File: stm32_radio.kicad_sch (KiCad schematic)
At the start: 3 parts, among them J1 Conn_01x03_Pin, J2 Conn_Coaxial_Small

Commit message: Almost ready for production
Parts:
- J1: LCSC (none) -> C49257
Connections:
- no-connect marks 25 -> 23
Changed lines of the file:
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@@
 	)
 	(junction
-		(at 38.1 143.51)
+		(at 66.04 110.49)
 		(diameter 0)
 		(color 0 0 0 0)
@@
 	)
 	(no_connect
-		(at 60.96 62.23)
-	)
-	(no_connect
 		(at 60.96 73.66)
 	)
@@
 	)
 	(no_connect
-		(at 60.96 59.69)
-	)
-	(no_connect
 		(at 60.96 76.2)
 	)
@@
 	(wire
 		(pts
-			(xy 38.1 143.51) (xy 38.1 144.78)
+			(xy 38.1 139.7) (xy 38.1 144.78)
 		)
 		(stroke
@@
 		(pts
 			(xy 60.96 119.38) (xy 71.12 119.38)
-		)
-		(stroke
-			(width 0)
-			(type default)
-		)
-	)
-	(wire
-		(pts
-			(xy 38.1 139.7) (xy 38.1 143.51)
 		)
 		(stroke
@@
 	)
 	(symbol
-		(lib_id "Connector:Conn_01x03_Pin")
-		(at 71.12 105.41 270)
+		(lib_id "power:PWR_FLAG")
+		(at 66.04 110.49 0)
 		(unit 1)
 		(exclude_from_sim no)
@@
 		(dnp no)
 		(fields_autoplaced yes)
-		(property "Reference" "J1"
-			(at 71.12 100.33 90)
-			(effects
-				(font
-					(size 1.27 1.27)
-				)
-			)
-		)
-		(property "Value" "Conn_01x03_Pin"
-			(at 71.12 102.87 90)
-			(effects
-				(font
-					(size 1.27 1.27)
-				)
-			)
-		)
-		(property "Footprint" "Connector_PinHeader_2.54mm:PinHeader_1x03_P2.54mm_Vertical"
-			(at 71.12 105.41 0)
+		(property "Reference" "#FLG05"
+			(at 66.04 108.585 0)
+			(effects
+				(font
+					(size 1.27 1.27)
+				)
+				(hide yes)
+			)
+		)
+		(property "Value" "PWR_FLAG"
+			(at 66.04 105.41 0)
+			(effects
+				(font
+					(size 1.27 1.27)
+				)
+			)
+		)
+		(property "Footprint" ""
+			(at 66.04 110.49 0)
 			(effects
 				(font
@@
 		)
 		(property "Datasheet" "~"
-			(at 71.12 105.41 0)
-			(effects
-				(font
-					(size 1.27 1.27)
-				)
-				(hide yes)
-			)
-		)
-		(property "Description" "Generic connector, single row, 01x03, script generated"
-			(at 71.12 105.41 0)
+			(at 66.04 110.49 0)
+			(effects
+				(font
+					(size 1.27 1.27)
+				)
+				(hide yes)
+			)
+		)
+		(property "Description" "Special symbol for telling ERC where power comes from"
+			(at 66.04 110.49 0)
 			(effects
 				(font
@@
 		(pin "1"
 		)
-		(pin "3"
-		)
-		(pin "2"
-		)
 		(instances
-			(project ""
+			(project "stm32_radio"
 				(path "/432d5beb-0309-422b-bb62-0445459d5147"
-					(reference "J1")
+					(reference "#FLG05")
 					(unit 1)
 				)
@@
 	)
 	(symbol
-		(lib_id "power:PWR_FLAG")
-		(at 38.1 143.51 90)
+		(lib_id "Connector:Conn_01x03_Pin")
+		(at 71.12 105.41 270)
 		(unit 1)
 		(exclude_from_sim no)
@@
 		(dnp no)
 		(fields_autoplaced yes)
-		(property "Reference" "#FLG01"
-			(at 36.195 143.51 0)
-			(effects
-				(font
-					(size 1.27 1.27)
-				)
-				(hide yes)
-			)
-		)
-		(property "Value" "PWR_FLAG"
-			(at 34.29 143.5099 90)
-			(effects
-				(font
-					(size 1.27 1.27)
-				)
-				(justify left)
-			)
-		)
-		(property "Footprint" ""
-			(at 38.1 143.51 0)
+		(property "Reference" "J1"
+			(at 71.12 100.33 90)
+			(effects
+				(font
+					(size 1.27 1.27)
+				)
+			)
+		)
+		(property "Value" "Conn_01x03_Pin"
+			(at 71.12 102.87 90)
+			(effects
+				(font
+					(size 1.27 1.27)
+				)
+			)
+		)
+		(property "Footprint" "Connector_PinHeader_2.54mm:PinHeader_1x03_P2.54mm_Vertical"
+			(at 71.12 105.41 0)
 			(effects
 				(font
@@
 		)
 		(property "Datasheet" "~"
-			(at 38.1 143.51 0)
-			(effects
-				(font
-					(size 1.27 1.27)
-				)
-				(hide yes)
-			)
-		)
-		(property "Description" "Special symbol for telling ERC where power comes from"
-			(at 38.1 143.51 0)
-			(effects
-				(font
-					(size 1.27 1.27)
-				)
-				(hide yes)
+			(at 71.12 105.41 0)
+			(effects
+				(font
+					(size 1.27 1.27)
+				)
+				(hide yes)
+			)
+		)
+		(property "Description" "Generic connector, single row, 01x03, script generated"
+			(at 71.12 105.41 0)
+			(effects
+				(font
+					(size 1.27 1.27)
+				)
+				(hide yes)
+			)
+		)
+		(property "LCSC" "C49257"
+			(at 71.12 105.41 0)
+			(effects
+				(font
+					(size 1.27 1.27)
+				)
 			)
 		)
 		(pin "1"
+		)
+		(pin "3"
+		)
+		(pin "2"
 		)
 		(instances
 			(project ""
 				(path "/432d5beb-0309-422b-bb62-0445459d5147"
-					(reference "#FLG01")
+					(reference "J1")
 					(unit 1)
 				)

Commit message: Finalize design
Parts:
- removed J1: Conn_01x03_Pin, Connector_PinHeader_2.54mm:PinHeader_1x03_P2.54mm_Vertical, symbol Connector:Conn_01x03_Pin

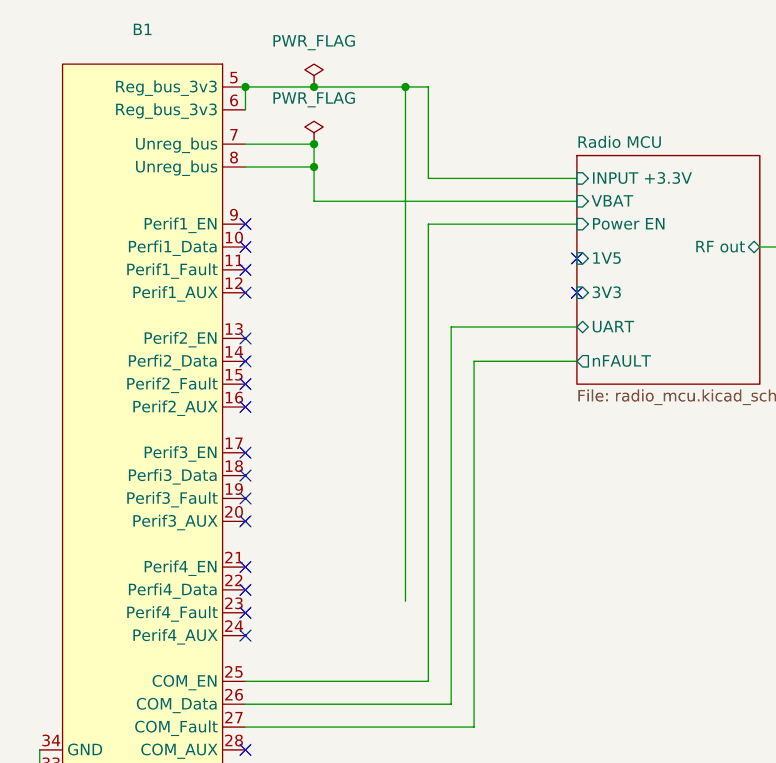
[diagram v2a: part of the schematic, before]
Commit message: Altered LCSC part numbers according to current stock
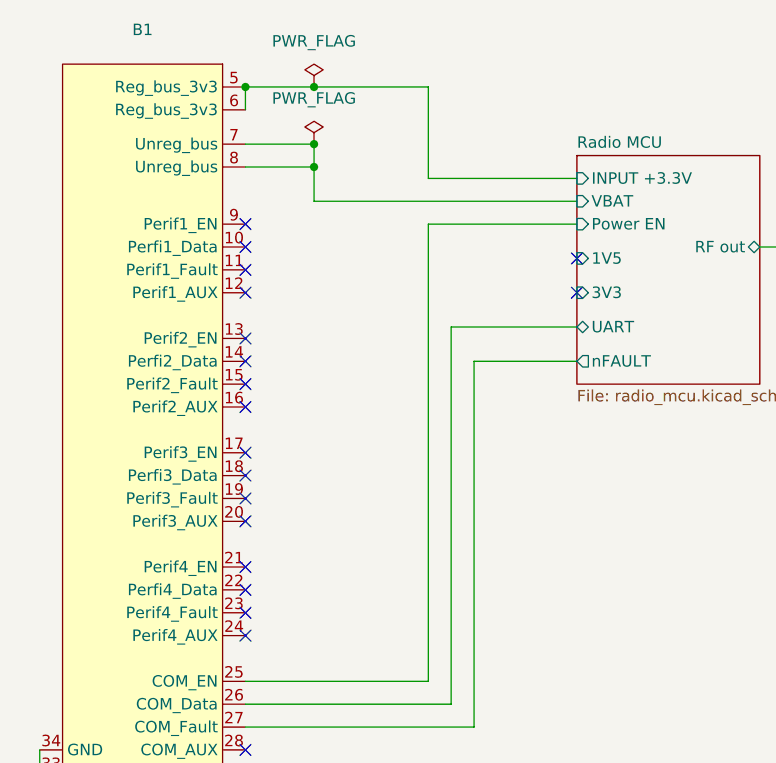
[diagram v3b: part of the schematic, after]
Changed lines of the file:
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@@
-	)
-	(junction
-		(at 78.74 53.34)
-		(diameter 0)
-		(color 0 0 0 0)
 	)
 	(junction
@@
 	(wire
 		(pts
-			(xy 68.58 53.34) (xy 78.74 53.34)
-		)
-		(stroke
-			(width 0)
-			(type default)
-		)
-	)
-	(wire
-		(pts
 			(xy 138.43 71.12) (xy 138.43 72.39)
 		)
@@
 	(wire
 		(pts
-			(xy 78.74 53.34) (xy 78.74 110.49)
-		)
-		(stroke
-			(width 0)
-			(type default)
-		)
-	)
-	(wire
-		(pts
 			(xy 83.82 80.01) (xy 97.79 80.01)
 		)
@@
 	(wire
 		(pts
-			(xy 81.28 53.34) (xy 78.74 53.34)
+			(xy 68.58 53.34) (xy 81.28 53.34)
 		)
 		(stroke

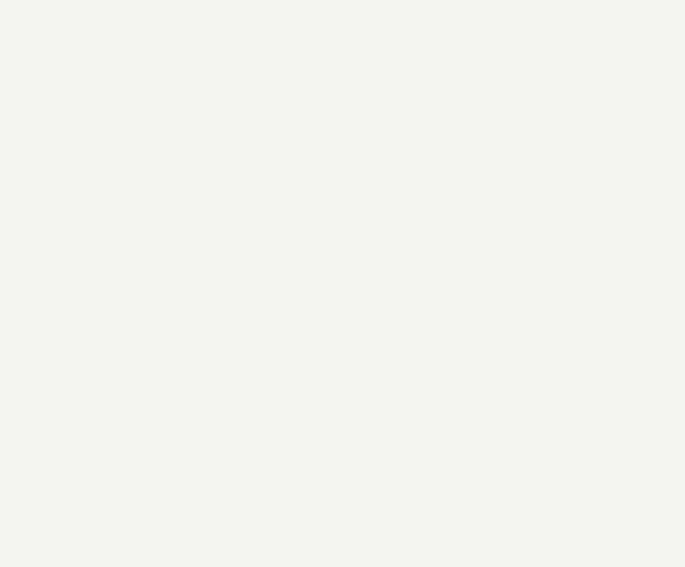
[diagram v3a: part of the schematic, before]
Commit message: Added a pair of SMA connectors for measurement
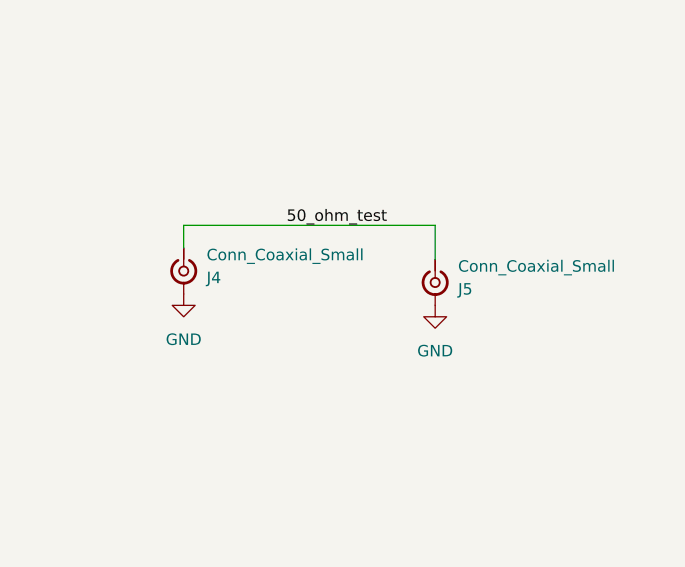
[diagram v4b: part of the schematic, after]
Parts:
- added J4, J5: Conn_Coaxial_Small, Connector_Coaxial:SMA_Samtec_SMA-J-P-H-ST-EM1_EdgeMount, symbol Connector:Conn_Coaxial_Small
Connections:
- net GND: now also J4.2 (Ext), J5.2 (Ext)
- new net 50_ohm_test: J4.1 (In), J5.1 (In)
